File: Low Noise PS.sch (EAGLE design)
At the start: 70 parts, among them IC1 MAX6350SO08, IC2 OP27, IC3 LT1677, IC4 LT1677, IC5 MC79M12CDTG, IC6 MC78M12BDTG, Q1 MMBT2907AMMBTA56SOT23, Q2 MMBT5550SOT23, Q3 PMBF170, Q4 BSH201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

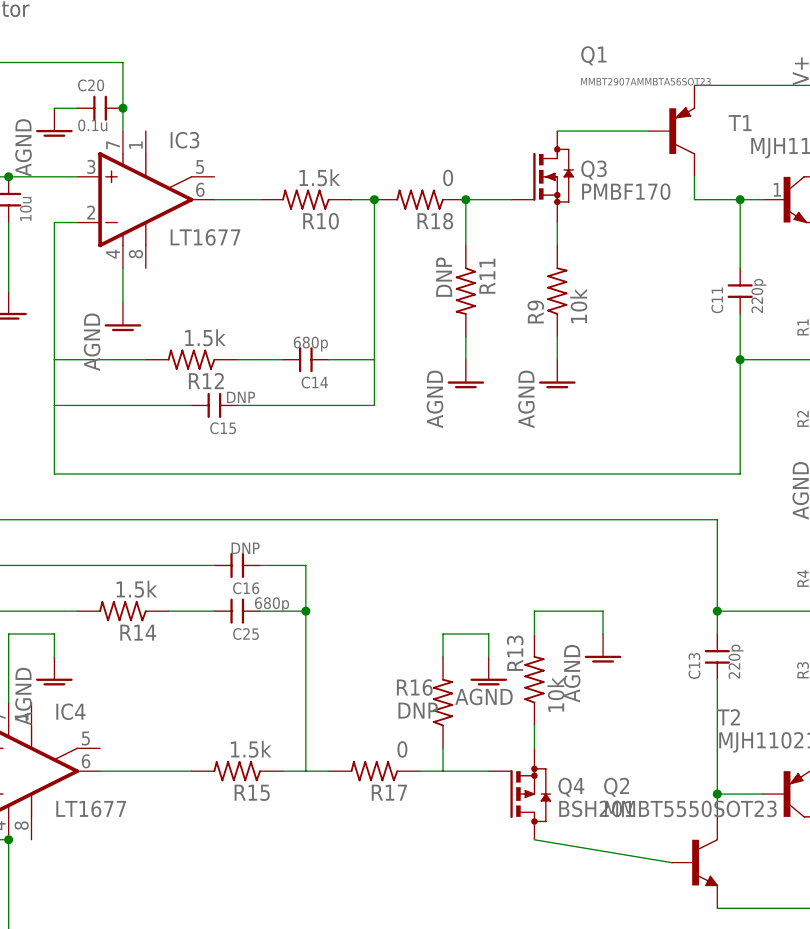
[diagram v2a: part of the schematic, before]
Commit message: Change in component values. Not final version!
After assembling commit 290fa40aa6a372085 the board oscillates.
Changing all DNP resistors and all 0 Ohm resistors to 1.5K Ohm makes the
positive regulator stable under 6 Ohm load. The negative section is
still unstable. Some final value adjustment will be required to ensure
unconditional stability (with enough margin to account for the variation
of capacitor values with temperature.
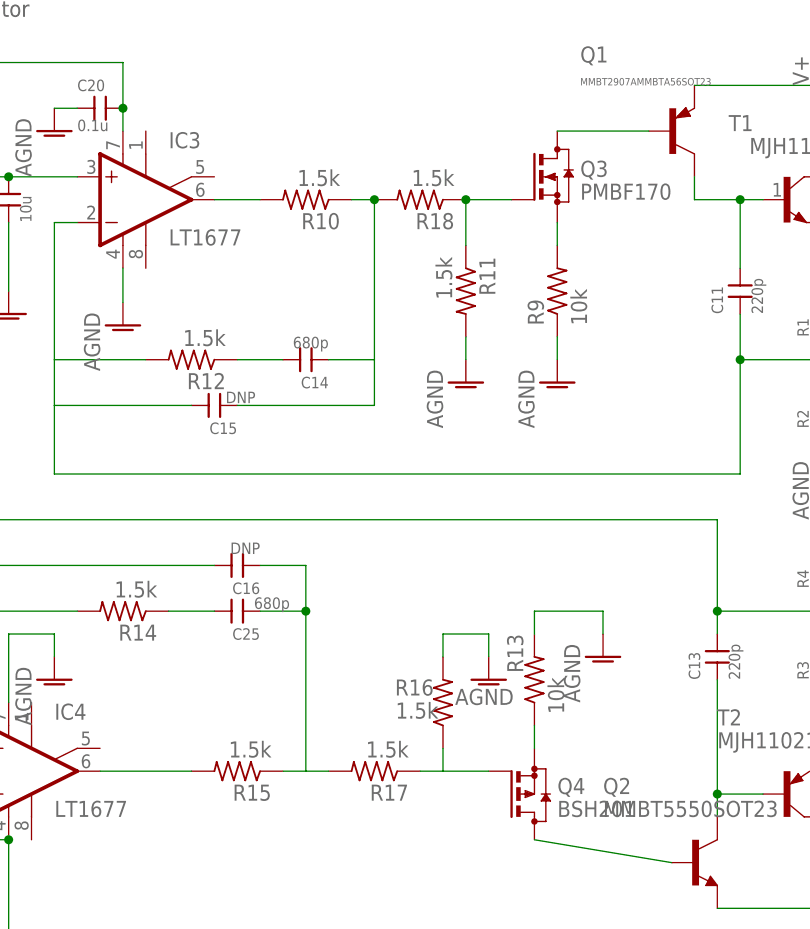
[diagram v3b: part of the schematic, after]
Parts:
- R11, R16: value DNP -> 1.5k; DIGIKEY (none) -> 541-1.5KECT-ND
- R17, R18: value 0 -> 1.5k; DIGIKEY RMCF1206ZT0R00CT-ND -> 541-1.5KECT-ND
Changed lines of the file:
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@@
 <attribute name="DIGIKEY" value="541-1.5KECT-ND"/>
 </part>
-<part name="R11" library="rcl" deviceset="R-US_" device="R1206" value="DNP"/>
+<part name="R11" library="rcl" deviceset="R-US_" device="R1206" value="1.5k">
+<attribute name="DIGIKEY" value="541-1.5KECT-ND"/>
+</part>
 <part name="AGND17" library="supply1" deviceset="AGND" device=""/>
 <part name="AGND20" library="supply1" deviceset="AGND" device=""/>
@@
 <attribute name="DIGIKEY" value="541-1.5KECT-ND"/>
 </part>
-<part name="R16" library="rcl" deviceset="R-US_" device="R1206" value="DNP"/>
+<part name="R16" library="rcl" deviceset="R-US_" device="R1206" value="1.5k">
+<attribute name="DIGIKEY" value="541-1.5KECT-ND"/>
+</part>
 <part name="AGND21" library="supply1" deviceset="AGND" device=""/>
 <part name="AGND22" library="supply1" deviceset="AGND" device=""/>
-<part name="R17" library="rcl" deviceset="R-US_" device="R1206" value="0">
-<attribute name="DIGIKEY" value="RMCF1206ZT0R00CT-ND"/>
-</part>
-<part name="R18" library="rcl" deviceset="R-US_" device="R1206" value="0">
-<attribute name="DIGIKEY" value="RMCF1206ZT0R00CT-ND"/>
+<part name="R17" library="rcl" deviceset="R-US_" device="R1206" value="1.5k">
+<attribute name="DIGIKEY" value="541-1.5KECT-ND"/>
+</part>
+<part name="R18" library="rcl" deviceset="R-US_" device="R1206" value="1.5k">
+<attribute name="DIGIKEY" value="541-1.5KECT-ND"/>
 </part>
 <part name="F1" library="jqi-power-supply" deviceset="FUSE" device="1206">
@@
 <attribute name="DIGIKEY" x="342.9" y="76.2" size="1.778" layer="96" rot="R180" display="off"/>
 </instance>
-<instance part="R11" gate="G$1" x="360.68" y="66.04" rot="R270"/>
+<instance part="R11" gate="G$1" x="360.68" y="66.04" rot="R270">
+<attribute name="DIGIKEY" x="360.68" y="66.04" size="1.778" layer="96" rot="R270" display="off"/>
+</instance>
 <instance part="AGND17" gate="VR1" x="370.84" y="55.88"/>
 <instance part="AGND20" gate="VR1" x="360.68" y="55.88"/>
@@
 <attribute name="NAME" x="357.124" y="22.8854" size="1.778" layer="95" rot="R180"/>
 <attribute name="VALUE" x="357.632" y="20.32" size="1.778" layer="96" rot="R180"/>
+<attribute name="DIGIKEY" x="358.14" y="20.32" size="1.778" layer="96" rot="R90" display="off"/>
 </instance>
 <instance part="AGND21" gate="VR1" x="375.92" y="25.4"/>
